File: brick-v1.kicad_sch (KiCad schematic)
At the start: 18 parts, among them J1 battery_header, U1 XBEE S2C PRO, U2 ESC, U3 ESC, U4 esp32, U5 L7805, U6 ESC, U7 ESC, U8 ULTRASONIC SENSOR, U9 Teensy4.1

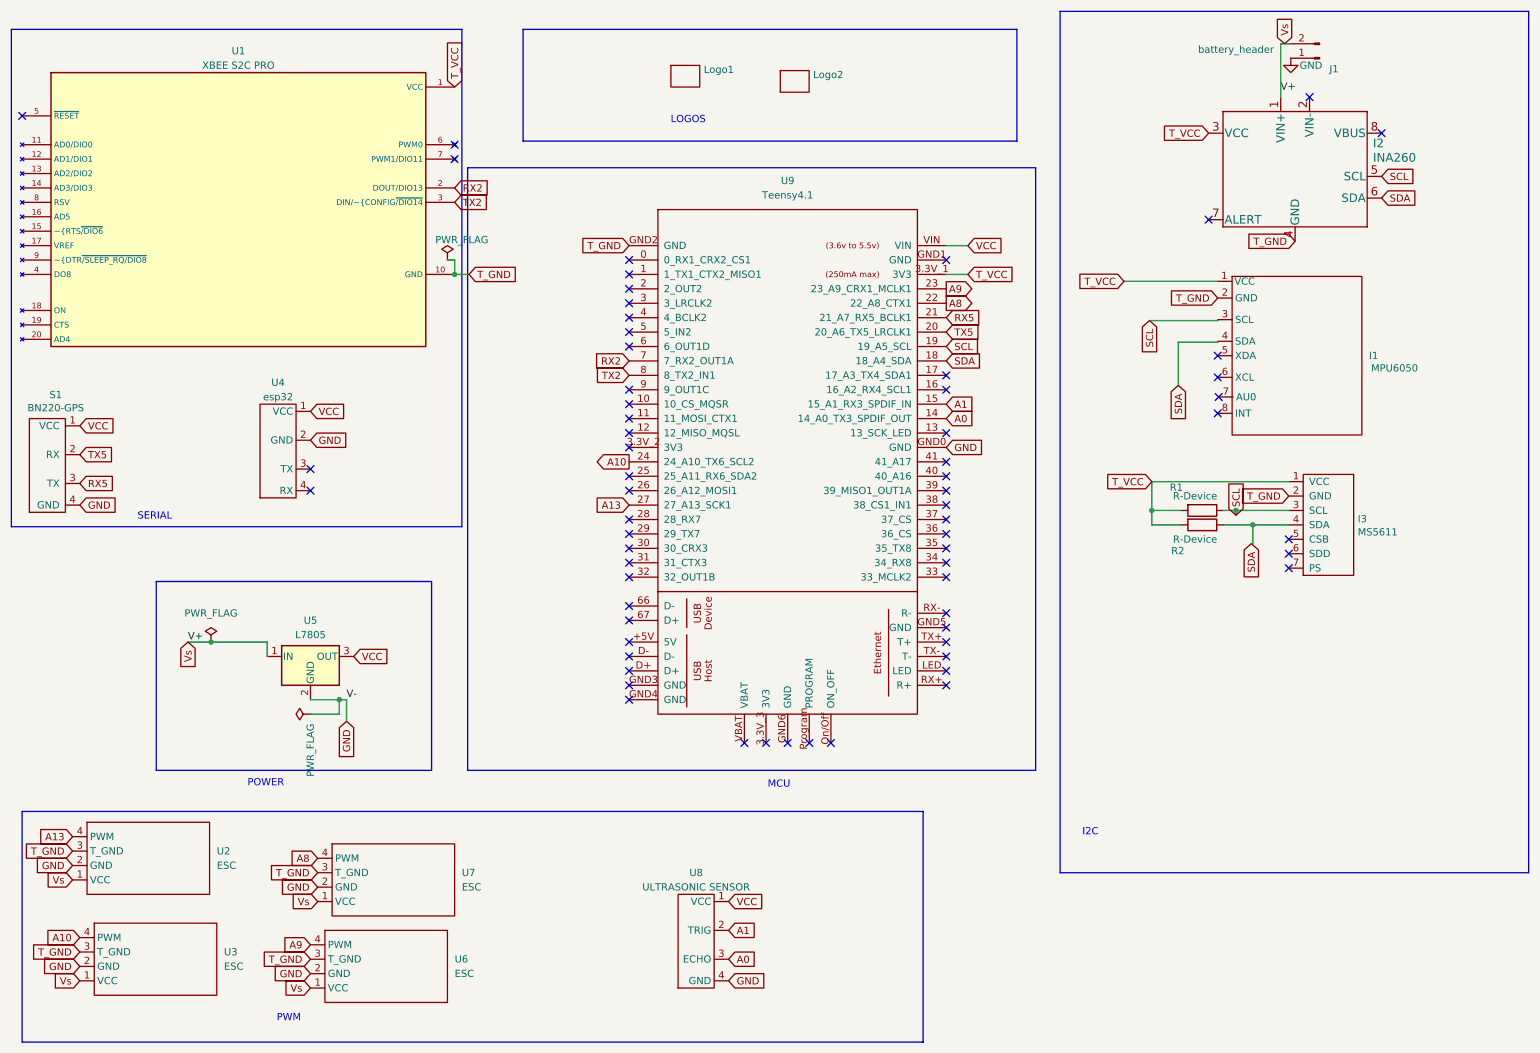
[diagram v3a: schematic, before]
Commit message: deleted and organized footprints
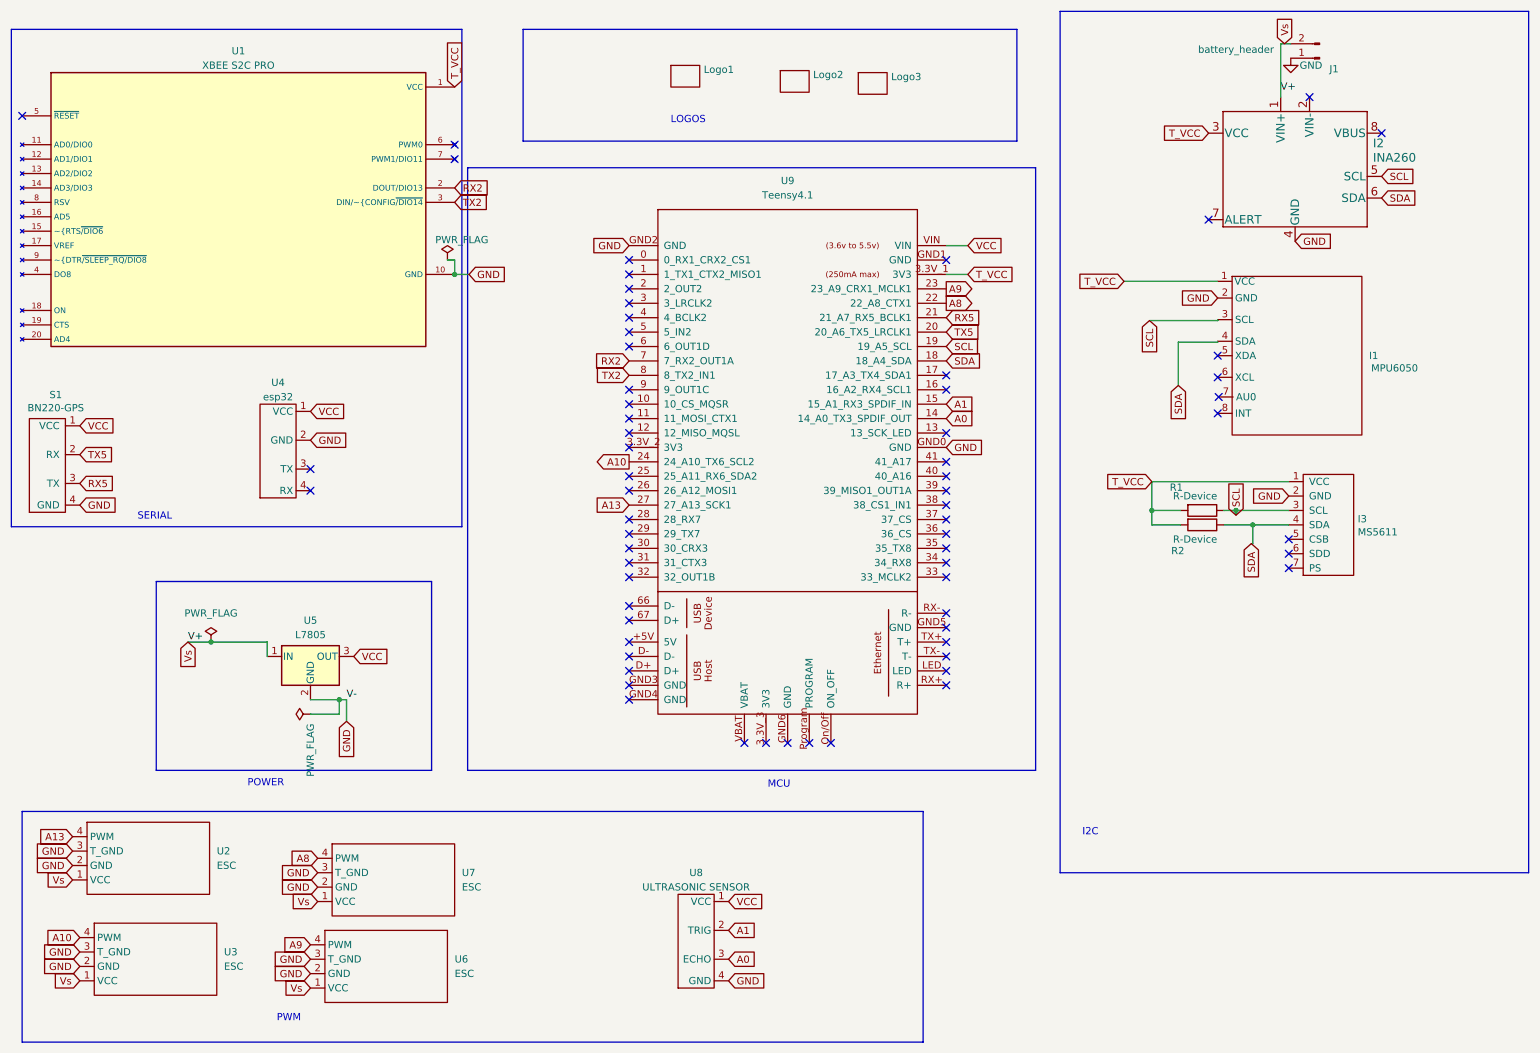
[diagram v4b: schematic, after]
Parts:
- added Logo3: ~, rrc_logo:Alessandro, symbol rrc_pcb-rescue:logo
- Logo2: footprint rrc_logo:picturae -> rrc_logo:MIMS
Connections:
- net T_GND is gone; now on net GND: I1.2 (GND), I2.4 (GND), I3.2 (GND), U1.10 (GND), U2.3 (T_GND), U3.3 (T_GND), U6.3 (T_GND), U7.3 (T_GND), U9.GND2 (GND)
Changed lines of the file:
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@@
 	(title_block
 		(title "Flight controller")
-		(date "2025-07-13")
-		(rev "1.4")
+		(date "2026-01-05")
+		(rev "1.6")
 		(company "MIMS lab")
 		(comment 1 "Thesis")
@@
 		)
 	)
+	(global_label "GND"
+		(shape input)
+		(at 25.4 161.29 180)
+		(fields_autoplaced yes)
+		(effects
+			(font
+				(size 1.27 1.27)
+			)
+			(justify right)
+		)
+		(property "Intersheetrefs" "${INTERSHEET_REFS}"
+			(at 19.1985 161.29 0)
+			(effects
+				(font
+					(size 1.27 1.27)
+				)
+				(justify right)
+				(hide yes)
+			)
+		)
+	)
 	(global_label "RX2"
 		(shape input)
@@
 		)
 	)
-	(global_label "T_GND"
-		(shape input)
-		(at 67.31 180.34 180)
-		(fields_autoplaced yes)
-		(effects
-			(font
-				(size 1.27 1.27)
-			)
-			(justify right)
-		)
-		(property "Intersheetrefs" "${INTERSHEET_REFS}"
-			(at 59.1733 180.34 0)
-			(effects
-				(font
-					(size 1.27 1.27)
-				)
-				(justify right)
-				(hide yes)
-			)
-		)
-	)
 	(global_label "A8"
 		(shape input)
@@
 		)
 	)
+	(global_label "GND"
+		(shape input)
+		(at 95.25 59.69 0)
+		(fields_autoplaced yes)
+		(effects
+			(font
+				(size 1.27 1.27)
+			)
+			(justify left)
+		)
+		(property "Intersheetrefs" "${INTERSHEET_REFS}"
+			(at 101.4515 59.69 0)
+			(effects
+				(font
+					(size 1.27 1.27)
+				)
+				(justify left)
+				(hide yes)
+			)
+		)
+	)
 	(global_label "RX5"
 		(shape input)
@@
 		)
 	)
+	(global_label "GND"
+		(shape input)
+		(at 123.444 54.61 180)
+		(fields_autoplaced yes)
+		(effects
+			(font
+				(size 1.27 1.27)
+			)
+			(justify right)
+		)
+		(property "Intersheetrefs" "${INTERSHEET_REFS}"
+			(at 117.2425 54.61 0)
+			(effects
+				(font
+					(size 1.27 1.27)
+				)
+				(justify right)
+				(hide yes)
+			)
+		)
+	)
 	(global_label "SCL"
 		(shape input)
@@
 		)
 	)
-	(global_label "T_GND"
+	(global_label "GND"
 		(shape input)
-		(at 123.444 54.61 180)
+		(at 67.31 180.34 180)
 		(fields_autoplaced yes)
 		(effects
@@
 		)
 		(property "Intersheetrefs" "${INTERSHEET_REFS}"
-			(at 115.3073 54.61 0)
+			(at 61.1085 180.34 0)
 			(effects
 				(font
@@
 	(global_label "GND"
 		(shape input)
+		(at 68.58 165.1 180)
+		(fields_autoplaced yes)
+		(effects
+			(font
+				(size 1.27 1.27)
+			)
+			(justify right)
+		)
+		(property "Intersheetrefs" "${INTERSHEET_REFS}"
+			(at 62.3785 165.1 0)
+			(effects
+				(font
+					(size 1.27 1.27)
+				)
+				(justify right)
+				(hide yes)
+			)
+		)
+	)
+	(global_label "GND"
+		(shape input)
 		(at 26.67 100.33 0)
 		(fields_autoplaced yes)
@@
 		)
 	)
-	(global_label "T_GND"
-		(shape input)
-		(at 239.679 98.7358 180)
-		(fields_autoplaced yes)
-		(effects
-			(font
-				(size 1.27 1.27)
-			)
-			(justify right)
-		)
-		(property "Intersheetrefs" "${INTERSHEET_REFS}"
-			(at 231.5423 98.7358 0)
-			(effects
-				(font
-					(size 1.27 1.27)
-				)
-				(justify right)
-				(hide yes)
-			)
-		)
-	)
-	(global_label "T_GND"
-		(shape input)
-		(at 68.58 165.1 180)
-		(fields_autoplaced yes)
-		(effects
-			(font
-				(size 1.27 1.27)
-			)
-			(justify right)
-		)
-		(property "Intersheetrefs" "${INTERSHEET_REFS}"
-			(at 60.4433 165.1 0)
-			(effects
-				(font
-					(size 1.27 1.27)
-				)
-				(justify right)
-				(hide yes)
-			)
-		)
-	)
 	(global_label "T_VCC"
 		(shape input)
@@
 		)
 	)
-	(global_label "T_GND"
+	(global_label "GND"
 		(shape input)
-		(at 95.25 59.69 0)
+		(at 227.1545 63.8459 180)
 		(fields_autoplaced yes)
 		(effects
@@
 				(size 1.27 1.27)
 			)
-			(justify left)
+			(justify right)
 		)
 		(property "Intersheetrefs" "${INTERSHEET_REFS}"
-			(at 103.3867 59.69 0)
+			(at 220.953 63.8459 0)
 			(effects
 				(font
 					(size 1.27 1.27)
 				)
-				(justify left)
+				(justify right)
 				(hide yes)
 			)
@@
 		)
 	)
+	(global_label "GND"
+		(shape input)
+		(at 239.679 98.7358 180)
+		(fields_autoplaced yes)
+		(effects
+			(font
+				(size 1.27 1.27)
+			)
+			(justify right)
+		)
+		(property "Intersheetrefs" "${INTERSHEET_REFS}"
+			(at 233.4775 98.7358 0)
+			(effects
+				(font
+					(size 1.27 1.27)
+				)
+				(justify right)
+				(hide yes)
+			)
+		)
+	)
 	(global_label "A1"
 		(shape input)
@@
 		)
 	)
-	(global_label "T_GND"
-		(shape input)
-		(at 25.4 161.29 180)
-		(fields_autoplaced yes)
-		(effects
-			(font
-				(size 1.27 1.27)
-			)
-			(justify right)
-		)
-		(property "Intersheetrefs" "${INTERSHEET_REFS}"
-			(at 17.2633 161.29 0)
-			(effects
-				(font
-					(size 1.27 1.27)
-				)
-				(justify right)
-				(hide yes)
-			)
-		)
-	)
 	(global_label "GND"
 		(shape input)
@@
 		)
 	)
-	(global_label "T_GND"
-		(shape input)
-		(at 227.1545 63.8459 180)
-		(fields_autoplaced yes)
-		(effects
-			(font
-				(size 1.27 1.27)
-			)
-			(justify right)
-		)
-		(property "Intersheetrefs" "${INTERSHEET_REFS}"
-			(at 219.0178 63.8459 0)
-			(effects
-				(font
-					(size 1.27 1.27)
-				)
-				(justify right)
-				(hide yes)
-			)
-		)
-	)
 	(global_label "A9"
 		(shape input)
@@
 		)
 	)
-	(global_label "T_GND"
+	(global_label "GND"
 		(shape input)
-		(at 26.67 179.07 180)
+		(at 240.792 53.848 0)
 		(fields_autoplaced yes)
 		(effects
@@
 				(size 1.27 1.27)
 			)
-			(justify right)
+			(justify left)
 		)
 		(property "Intersheetrefs" "${INTERSHEET_REFS}"
-			(at 18.5333 179.07 0)
+			(at 246.9935 53.848 0)
 			(effects
 				(font
 					(size 1.27 1.27)
 				)
-				(justify right)
+				(justify left)
 				(hide yes)
 			)
 		)
 	)
-	(global_label "T_GND"
+	(global_label "Vs"
 		(shape input)
-		(at 240.792 53.848 180)
+		(at 45.72 124.46 270)
 		(fields_autoplaced yes)
 		(effects
@@
 		)
 		(property "Intersheetrefs" "${INTERSHEET_REFS}"
-			(at 232.6553 53.848 0)
+			(at 45.72 128.9077 90)
 			(effects
 				(font
@@
 		)
 	)
-	(global_label "Vs"
+	(global_label "GND"
 		(shape input)
-		(at 45.72 124.46 270)
+		(at 26.67 181.61 180)
 		(fields_autoplaced yes)
 		(effects
@@
 		)
 		(property "Intersheetrefs" "${INTERSHEET_REFS}"
-			(at 45.72 128.9077 90)
+			(at 20.4685 181.61 0)
 			(effects
 				(font
@@
 	(global_label "GND"
 		(shape input)
-		(at 26.67 181.61 180)
+		(at 26.67 179.07 180)
 		(fields_autoplaced yes)
 		(effects
@@
 		)
 		(property "Intersheetrefs" "${INTERSHEET_REFS}"
-			(at 20.4685 181.61 0)
+			(at 20.4685 179.07 0)
 			(effects
 				(font
@@
 	)
 	(symbol
+		(lib_id "rrc_pcb-rescue:logo")
+		(at 166.37 25.4 0)
+		(unit 1)
+		(exclude_from_sim no)
+		(in_bom yes)
+		(on_board yes)
+		(dnp no)
+		(property "Reference" "Logo3"
+			(at 169.6212 24.8666 0)
+			(effects
+				(font
+					(size 1.27 1.27)
+				)
+				(justify left)
+			)
+		)
+		(property "Value" "~"
+			(at 169.6212 27.178 0)
+			(effects
+				(font
+					(size 1.27 1.27)
+				)
+				(justify left)
+			)
+		)
+		(property "Footprint" "rrc_logo:Alessandro"
+			(at 166.37 25.4 0)
+			(effects
+				(font
+					(size 1.27 1.27)
+				)
+				(hide yes)
+			)
+		)
+		(property "Datasheet" ""
+			(at 166.37 25.4 0)
+			(effects
+				(font
+					(size 1.27 1.27)
+				)
+				(hide yes)
+			)
+		)
+		(property "Description" ""
+			(at 166.37 25.4 0)
+			(effects
+				(font
+					(size 1.27 1.27)
+				)
+				(hide yes)
+			)
+		)
+		(instances
+			(project "brick-v1"
+				(path "/03c52831-5dc5-43c5-a442-8d23643b46fb"
+					(reference "Logo3")
+					(unit 1)
+				)
+			)
+		)
+	)
+	(symbol
 		(lib_id "parts:INA260")
 		(at 240.792 51.308 0)
@@
 			)
 		)
-		(property "Footprint" "rrc_logo:picturae"
+		(property "Footprint" "rrc_logo:MIMS"
 			(at 152.6276 25.0441 0)
 			(effects
